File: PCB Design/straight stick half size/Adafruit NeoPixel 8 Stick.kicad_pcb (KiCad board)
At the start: 2 copper layers, 36.2 x 21 mm, 6 parts, among them CN1 1X4SMT, CN2 1X4SMT

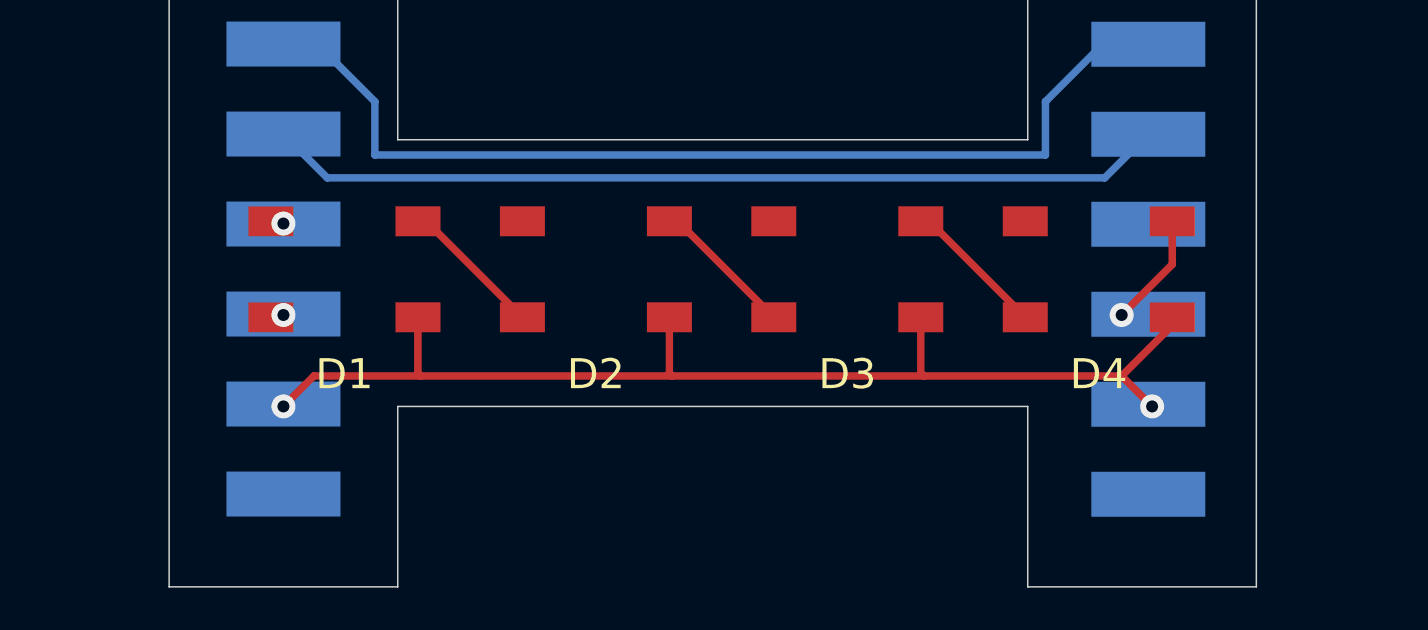
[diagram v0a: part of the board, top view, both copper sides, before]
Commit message: move vias off pads
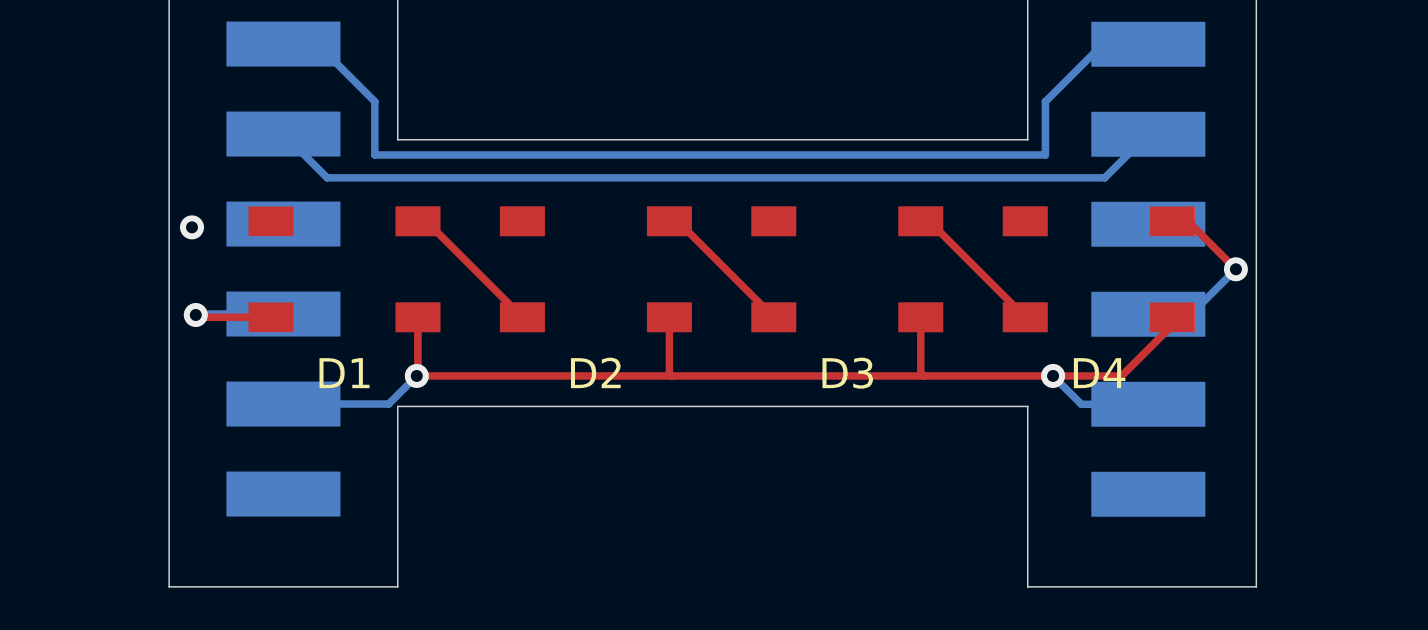
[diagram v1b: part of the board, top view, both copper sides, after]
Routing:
- net Net-(CN2-Pad3): track 0.00 -> 5.47 mm
- net Net-(D4-Pad2): track 3.82 -> 6.33 mm
- net +5V: track 38.4 -> 40.4 mm
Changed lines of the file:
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@@
   (segment (start 139.102 109.55) (end 139.102 111.416) (width 0.25) (layer "F.Cu") (net 1))
   (segment (start 147.484 109.55) (end 147.484 111.416) (width 0.25) (layer "F.Cu") (net 1))
-  (segment (start 127.254 111.506) (end 130.81 111.506) (width 0.25) (layer "F.Cu") (net 1))
   (segment (start 155.866 109.818) (end 154.178 111.506) (width 0.25) (layer "F.Cu") (net 1))
   (segment (start 130.72 109.55) (end 130.72 111.416) (width 0.25) (layer "F.Cu") (net 1))
   (segment (start 147.574 111.506) (end 154.178 111.506) (width 0.25) (layer "F.Cu") (net 1))
   (segment (start 139.102 111.416) (end 139.192 111.506) (width 0.25) (layer "F.Cu") (net 1))
-  (segment (start 126.238 112.522) (end 127.254 111.506) (width 0.25) (layer "F.Cu") (net 1))
   (segment (start 155.866 109.55) (end 155.866 109.818) (width 0.25) (layer "F.Cu") (net 1))
-  (segment (start 154.178 111.506) (end 155.194 112.522) (width 0.25) (layer "F.Cu") (net 1))
   (segment (start 130.72 111.416) (end 130.81 111.506) (width 0.25) (layer "F.Cu") (net 1))
   (segment (start 139.192 111.506) (end 147.574 111.506) (width 0.25) (layer "F.Cu") (net 1))
   (segment (start 147.484 111.416) (end 147.574 111.506) (width 0.25) (layer "F.Cu") (net 1))
-  (via (at 126.238 112.522) (size 0.8) (drill 0.4) (layers "F.Cu" "B.Cu") (net 1))
-  (via (at 155.194 112.522) (size 0.8) (drill 0.4) (layers "F.Cu" "B.Cu") (net 1))
-  (via (at 126.238 106.426) (size 0.8) (drill 0.4) (layers "F.Cu" "B.Cu") (net 2))
+  (via (at 130.683 111.506) (size 0.8) (drill 0.4) (layers "F.Cu" "B.Cu") (net 1))
+  (via (at 151.892 111.506) (size 0.8) (drill 0.4) (layers "F.Cu" "B.Cu") (net 1))
+  (segment (start 151.892 111.506) (end 152.836 112.45) (width 0.25) (layer "B.Cu") (net 1))
+  (segment (start 152.836 112.45) (end 155.067 112.45) (width 0.25) (layer "B.Cu") (net 1))
+  (segment (start 129.747 112.442) (end 130.683 111.506) (width 0.25) (layer "B.Cu") (net 1))
+  (segment (start 126.238 112.442) (end 129.747 112.442) (width 0.25) (layer "B.Cu") (net 1))
+  (via (at 123.19 106.553) (size 0.8) (drill 0.4) (layers "F.Cu" "B.Cu") (free) (net 2))
   (segment (start 153.615 104.902) (end 127.698 104.902) (width 0.25) (layer "B.Cu") (net 3))
   (segment (start 155.067 103.45) (end 153.615 104.902) (width 0.25) (layer "B.Cu") (net 3))
   (segment (start 127.698 104.902) (end 126.238 103.442) (width 0.25) (layer "B.Cu") (net 3))
-  (via (at 126.238 109.474) (size 0.8) (drill 0.4) (layers "F.Cu" "B.Cu") (net 4))
+  (segment (start 125.82 109.55) (end 123.393 109.55) (width 0.25) (layer "F.Cu") (net 4))
+  (segment (start 123.393 109.55) (end 123.317 109.474) (width 0.25) (layer "F.Cu") (net 4))
+  (via (at 123.317 109.474) (size 0.8) (drill 0.4) (layers "F.Cu" "B.Cu") (net 4))
+  (segment (start 126.238 109.442) (end 123.349 109.442) (width 0.25) (layer "B.Cu") (net 4))
+  (segment (start 123.349 109.442) (end 123.317 109.474) (width 0.25) (layer "B.Cu") (net 4))
   (segment (start 131.002 106.35) (end 134.202 109.55) (width 0.25) (layer "F.Cu") (net 5))
   (segment (start 130.72 106.35) (end 131.002 106.35) (width 0.25) (layer "F.Cu") (net 5))
@@
   (segment (start 147.766 106.35) (end 150.966 109.55) (width 0.25) (layer "F.Cu") (net 7))
   (segment (start 147.484 106.35) (end 147.766 106.35) (width 0.25) (layer "F.Cu") (net 7))
-  (segment (start 155.866 106.35) (end 155.866 107.786) (width 0.25) (layer "F.Cu") (net 8))
-  (segment (start 155.866 107.786) (end 154.178 109.474) (width 0.25) (layer "F.Cu") (net 8))
-  (via (at 154.178 109.474) (size 0.8) (drill 0.4) (layers "F.Cu" "B.Cu") (net 8))
+  (segment (start 156.388 106.35) (end 157.988 107.95) (width 0.25) (layer "F.Cu") (net 8))
+  (segment (start 155.866 106.35) (end 156.388 106.35) (width 0.25) (layer "F.Cu") (net 8))
+  (via (at 157.988 107.95) (size 0.8) (drill 0.4) (layers "F.Cu" "B.Cu") (net 8))
+  (segment (start 155.067 109.45) (end 156.488 109.45) (width 0.25) (layer "B.Cu") (net 8))
+  (segment (start 156.488 109.45) (end 157.988 107.95) (width 0.25) (layer "B.Cu") (net 8))
   (segment (start 153.55 100.45) (end 155.067 100.45) (width 0.25) (layer "B.Cu") (net 9))
   (segment (start 129.286 104.14) (end 151.638 104.14) (width 0.25) (layer "B.Cu") (net 9))
